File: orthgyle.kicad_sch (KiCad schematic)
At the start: 43 parts, among them J1 USB, J2 AVR_ISP_6, J3 JST, U1 ATMEGA328-PU, Y1 16MHz

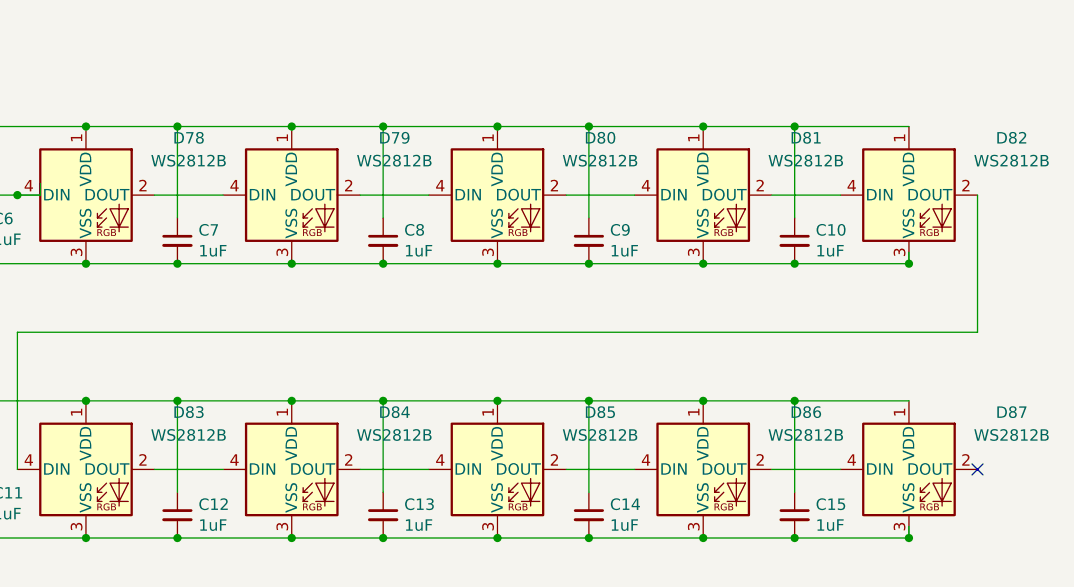
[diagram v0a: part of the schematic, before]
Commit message: Rename RGB diodes
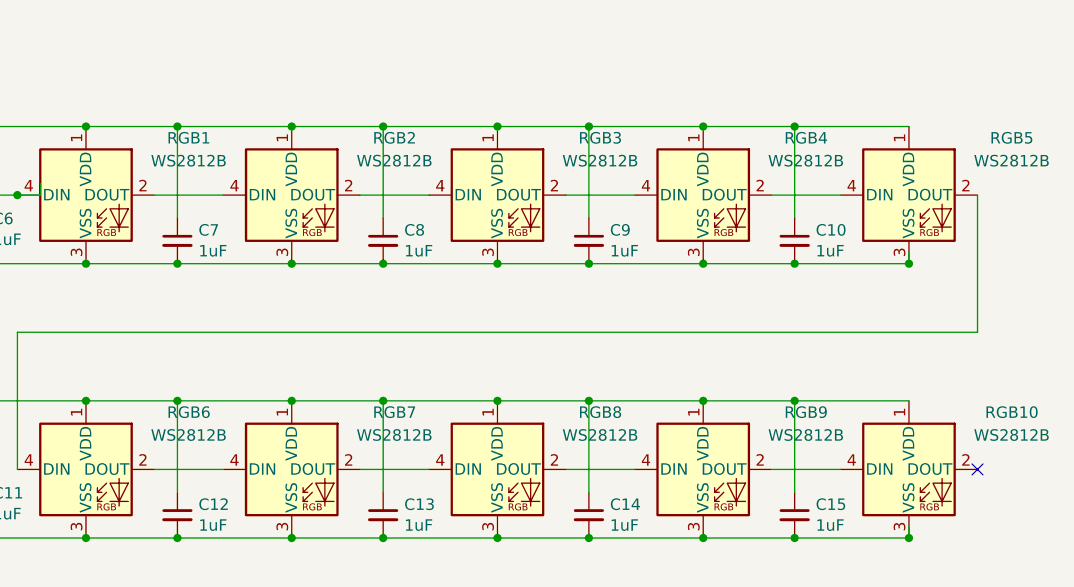
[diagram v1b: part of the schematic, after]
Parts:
- renumbered D78 to RGB1, D87 to RGB10, D79 to RGB2, D80 to RGB3, D81 to RGB4, D82 to RGB5, D83 to RGB6, D84 to RGB7, D85 to RGB8, D86 to RGB9
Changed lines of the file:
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@@
 	(title_block
 		(title "Orthgyle PCB")
-		(date "2024-12-16")
+		(date "2025-01-05")
 		(rev "1")
 	)
@@
 		(dnp no)
 		(fields_autoplaced yes)
-		(property "Reference" "D83"
+		(property "Reference" "RGB6"
 			(at 175.26 63.5314 0)
 			(effects
@@
 			(project "orthgyle"
 				(path "/463a010a-2077-405d-89e9-7586d05a9595"
-					(reference "D83")
+					(reference "RGB6")
 					(unit 1)
 				)
@@
 		(dnp no)
 		(fields_autoplaced yes)
-		(property "Reference" "D84"
+		(property "Reference" "RGB7"
 			(at 198.12 63.5314 0)
 			(effects
@@
 			(project "orthgyle"
 				(path "/463a010a-2077-405d-89e9-7586d05a9595"
-					(reference "D84")
+					(reference "RGB7")
 					(unit 1)
 				)
@@
 		(dnp no)
 		(fields_autoplaced yes)
-		(property "Reference" "D86"
+		(property "Reference" "RGB9"
 			(at 243.84 63.5314 0)
 			(effects
@@
 			(project "orthgyle"
 				(path "/463a010a-2077-405d-89e9-7586d05a9595"
-					(reference "D86")
+					(reference "RGB9")
 					(unit 1)
 				)
@@
 		(dnp no)
 		(fields_autoplaced yes)
-		(property "Reference" "D80"
+		(property "Reference" "RGB3"
 			(at 220.98 33.0514 0)
 			(effects
@@
 			(project "orthgyle"
 				(path "/463a010a-2077-405d-89e9-7586d05a9595"
-					(reference "D80")
+					(reference "RGB3")
 					(unit 1)
 				)
@@
 		(dnp no)
 		(fields_autoplaced yes)
-		(property "Reference" "D85"
+		(property "Reference" "RGB8"
 			(at 220.98 63.5314 0)
 			(effects
@@
 			(project "orthgyle"
 				(path "/463a010a-2077-405d-89e9-7586d05a9595"
-					(reference "D85")
+					(reference "RGB8")
 					(unit 1)
 				)
@@
 		(dnp no)
 		(fields_autoplaced yes)
-		(property "Reference" "D81"
+		(property "Reference" "RGB4"
 			(at 243.84 33.0514 0)
 			(effects
@@
 			(project "orthgyle"
 				(path "/463a010a-2077-405d-89e9-7586d05a9595"
-					(reference "D81")
+					(reference "RGB4")
 					(unit 1)
 				)
@@
 		(dnp no)
 		(fields_autoplaced yes)
-		(property "Reference" "D78"
+		(property "Reference" "RGB1"
 			(at 175.26 33.0514 0)
 			(effects
@@
 			(project ""
 				(path "/463a010a-2077-405d-89e9-7586d05a9595"
-					(reference "D78")
+					(reference "RGB1")
 					(unit 1)
 				)
@@
 		(dnp no)
 		(fields_autoplaced yes)
-		(property "Reference" "D79"
+		(property "Reference" "RGB2"
 			(at 198.12 33.0514 0)
 			(effects
@@
 			(project "orthgyle"
 				(path "/463a010a-2077-405d-89e9-7586d05a9595"
-					(reference "D79")
+					(reference "RGB2")
 					(unit 1)
 				)
@@
 		(dnp no)
 		(fields_autoplaced yes)
-		(property "Reference" "D82"
+		(property "Reference" "RGB5"
 			(at 266.7 33.0514 0)
 			(effects
@@
 			(project "orthgyle"
 				(path "/463a010a-2077-405d-89e9-7586d05a9595"
-					(reference "D82")
+					(reference "RGB5")
 					(unit 1)
 				)
@@
 		(dnp no)
 		(fields_autoplaced yes)
-		(property "Reference" "D87"
+		(property "Reference" "RGB10"
 			(at 266.7 63.5314 0)
 			(effects
@@
 			(project "orthgyle"
 				(path "/463a010a-2077-405d-89e9-7586d05a9595"
-					(reference "D87")
+					(reference "RGB10")
 					(unit 1)
 				)

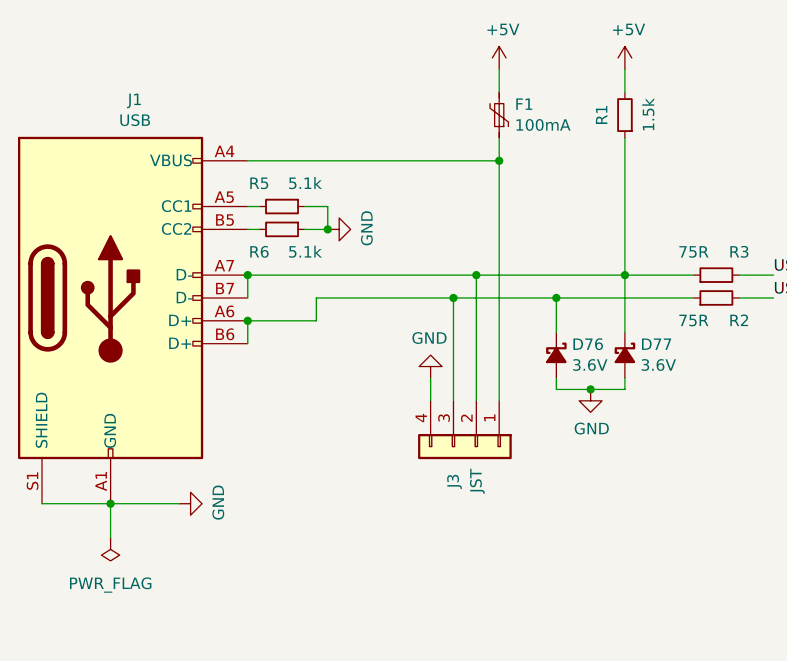
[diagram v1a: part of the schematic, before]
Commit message: Align USB port with case location
Switch to SK6812 mini-e LEDs
Flip stabilizer orientation
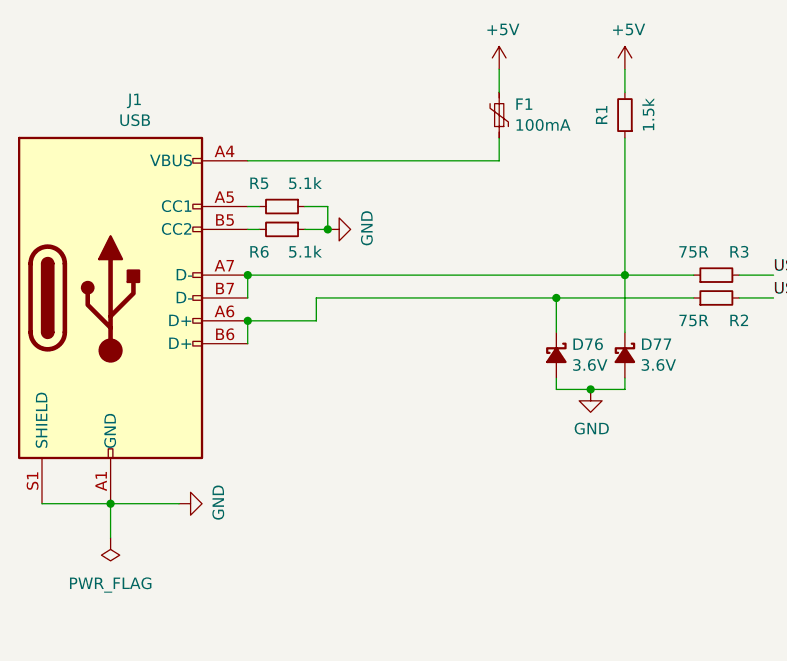
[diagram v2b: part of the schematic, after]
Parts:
- removed J3: JST, Connector_JST:JST_SH_SM04B-SRSS-TB_1x04-1MP_P1.00mm_Horizontal, symbol Connector_Generic:Conn_01x04
- RGB1, RGB10, RGB2, RGB3, RGB4, RGB5, RGB6, RGB7, RGB8, RGB9: footprint LED_SMD:LED_WS2812B_PLCC4_5.0x5.0mm_P3.2mm -> Orthgyle:SK6812-MINI-E

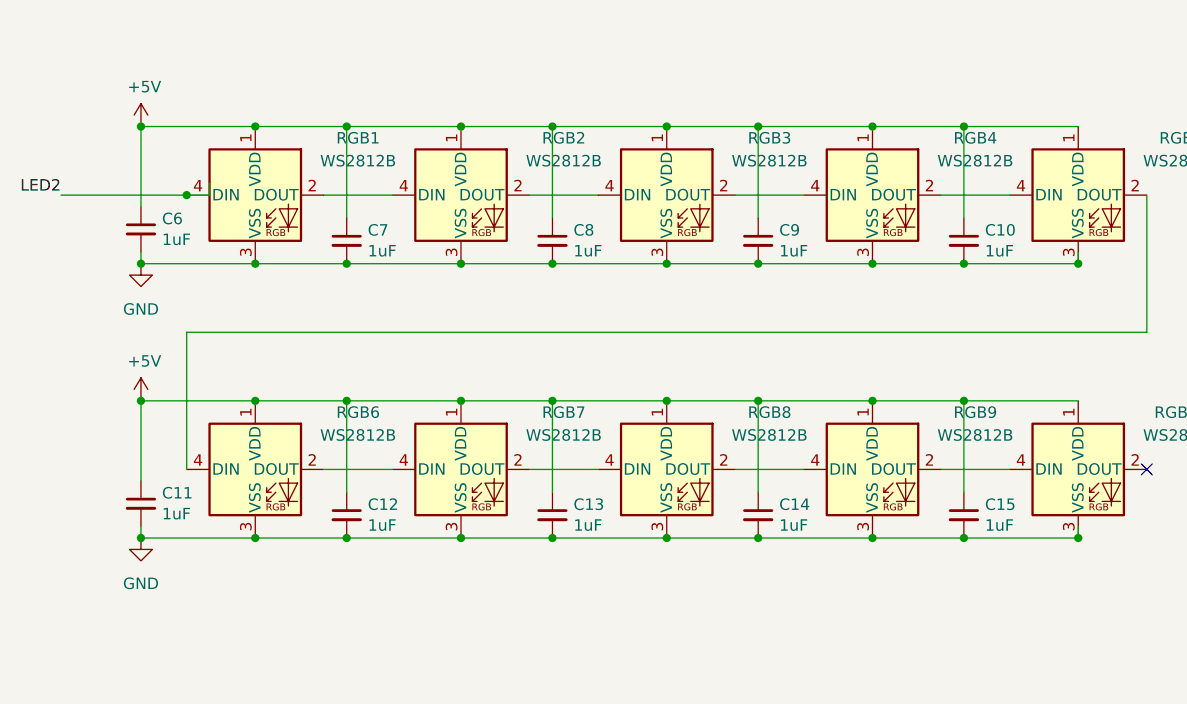
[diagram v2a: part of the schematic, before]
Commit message: Switch LEDs to SK6812-mini-e
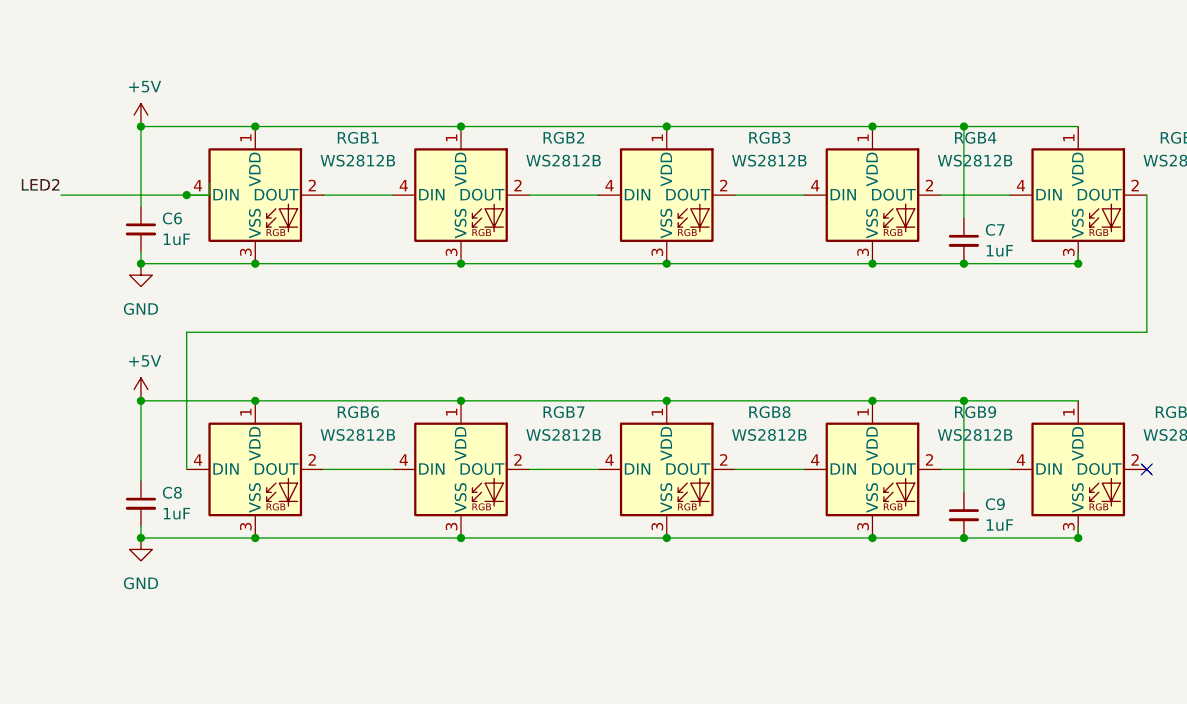
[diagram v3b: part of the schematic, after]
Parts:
- removed C12, C13, C14, C7, C8, C9: 1uF, Capacitor_THT:C_Disc_D4.3mm_W1.9mm_P5.00mm, symbol Device:C_Small
- renumbered C10 to C7, C11 to C8, C15 to C9

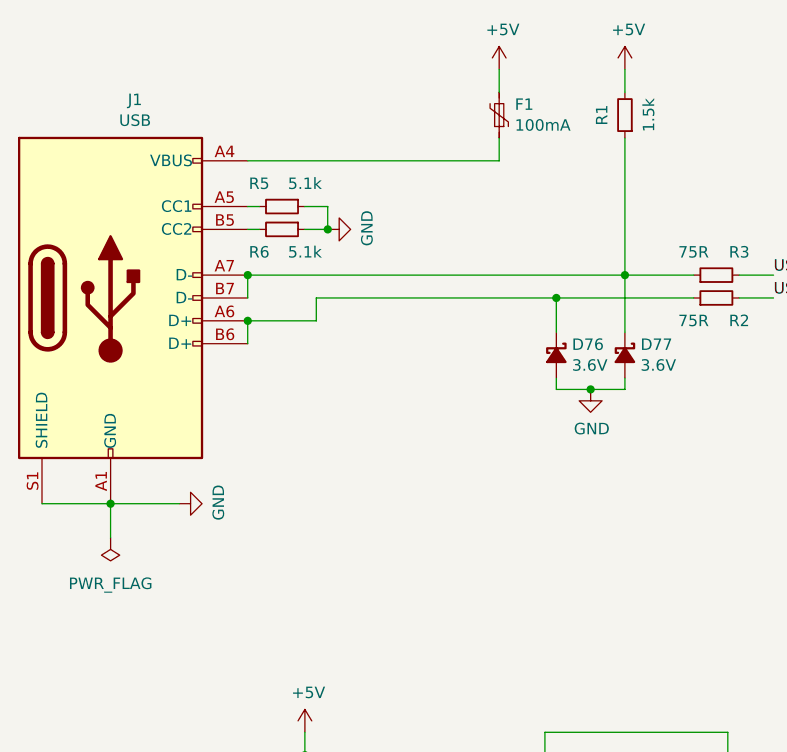
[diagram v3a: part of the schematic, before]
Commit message: Add center offset 2u keys
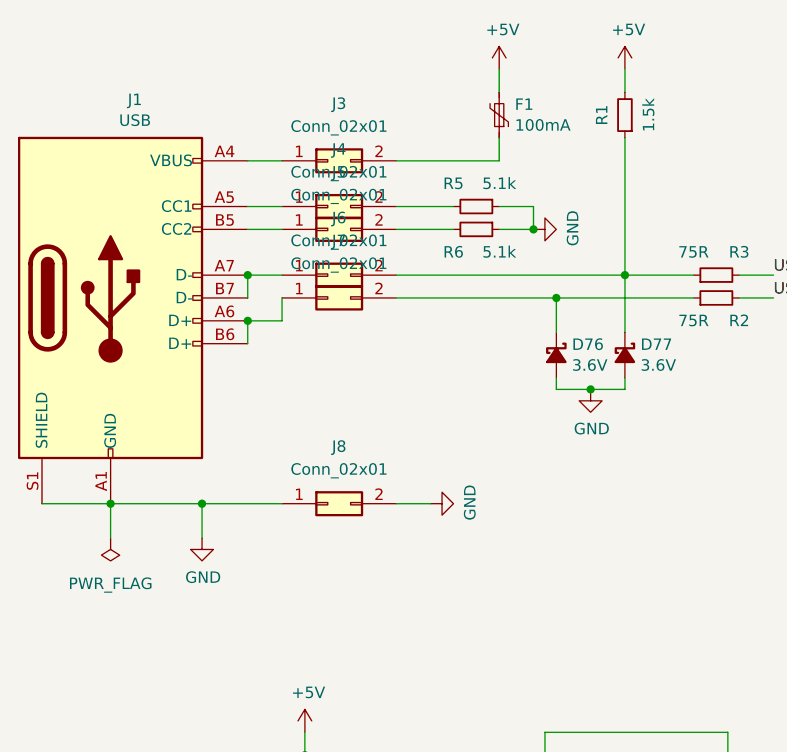
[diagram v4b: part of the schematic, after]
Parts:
- added J3, J4, J5, J6, J7, J8: Conn_02x01, Jumper:SolderJumper-2_P1.3mm_Bridged_RoundedPad1.0x1.5mm, symbol Connector_Generic:Conn_02x01
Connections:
- net GND: now also J8.1 (Pin_1), J8.2 (Pin_2)
- net at D76.1 (K), R2.1: now also J7.2 (Pin_2); no longer J1.A6 (D+), J1.B6 (D+)
- net at D77.1 (K), R1.1, R3.1: now also J6.2 (Pin_2); no longer J1.A7 (D-), J1.B7 (D-)
- net at J1.A4 (VBUS), J1.A9 (VBUS), J1.B4 (VBUS)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: now also J3.1 (Pin_1); no longer F1.1
- net at J1.A5 (CC1): now also J4.1 (Pin_1); no longer R5.2
- net at J1.B5 (CC2): now also J5.1 (Pin_1); no longer R6.2
- new net: F1.1, J3.2 (Pin_2)
- new net: J1.A6 (D+), J1.B6 (D+), J7.1 (Pin_1)
- new net: J1.A7 (D-), J1.B7 (D-), J6.1 (Pin_1)
- new net: J4.2 (Pin_2), R5.2
- new net: J5.2 (Pin_2), R6.2
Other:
- moved on the sheet: R5, R6
